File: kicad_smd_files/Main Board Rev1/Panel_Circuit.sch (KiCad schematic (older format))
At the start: 31 parts, among them J12 Conn_01x24_Male, Q1 MMBT3904-7-F, Q2 MMBT3904-7-F, SW2 LEFT/DOWN, SW3 OK, SW4 RIGHT/UP, SW5 MENU, U3 CD4006B

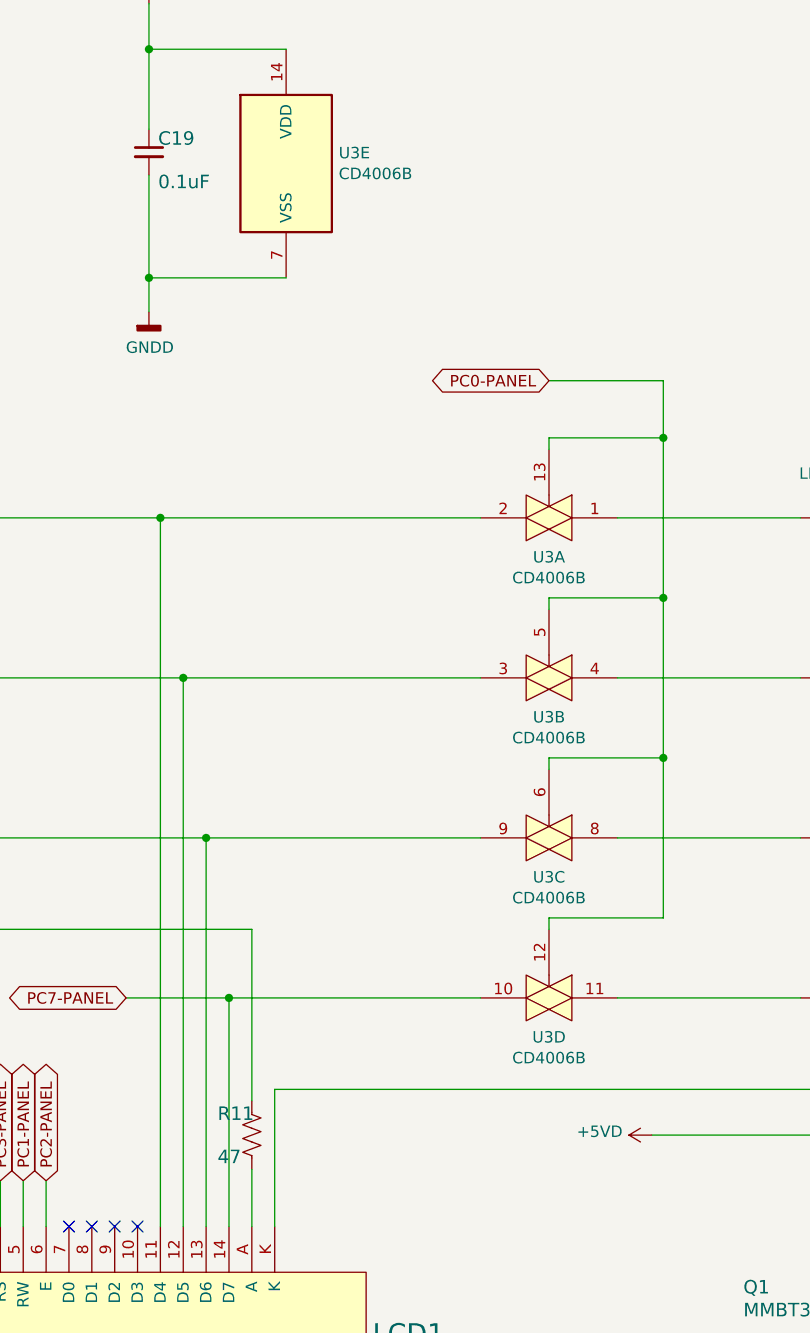
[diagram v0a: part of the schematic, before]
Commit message: Firmware patch to support new LCD, more beefy power circuit for LiPo, added LiPo Balance and protection, fixed reversed op-amp comparitor pins
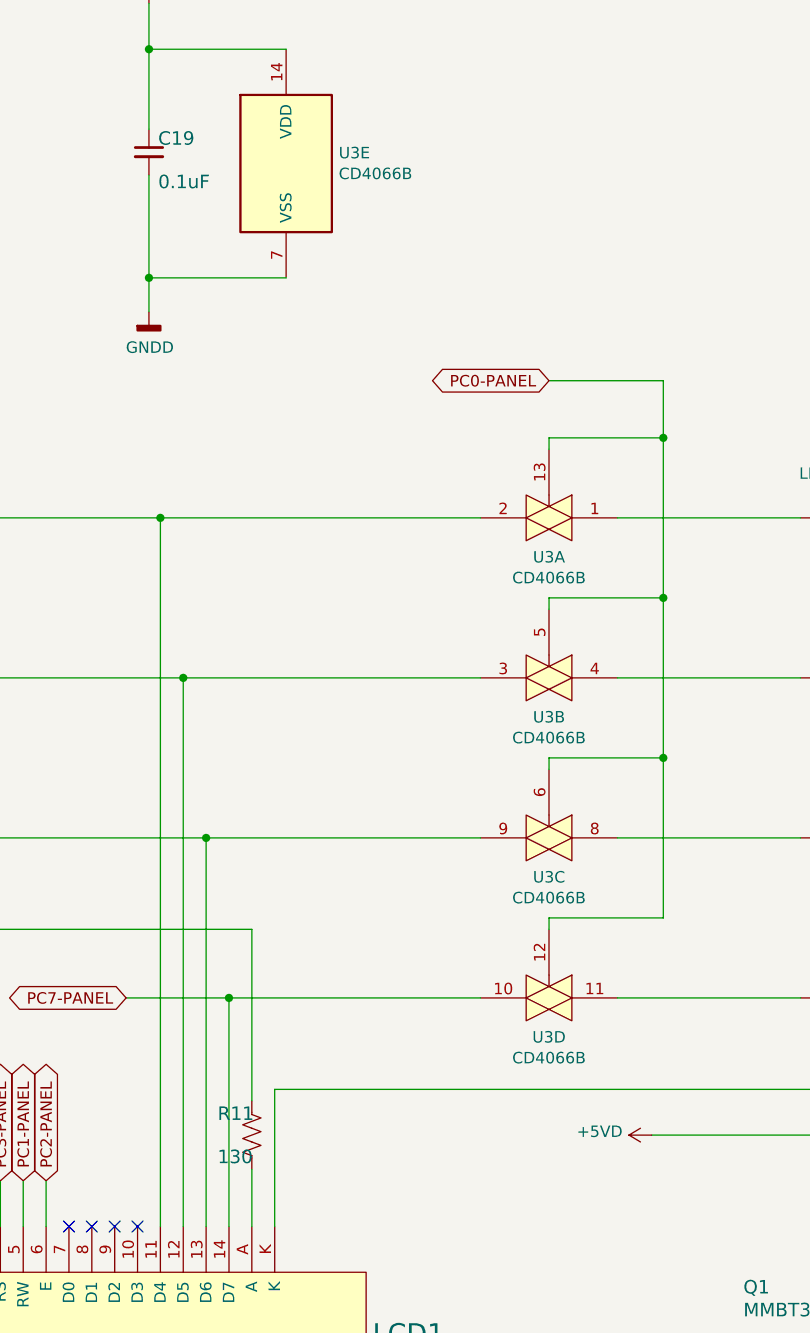
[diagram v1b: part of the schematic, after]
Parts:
- R11: value 47 -> 130; Manufacturer_Name Panasonic -> Yageo; Manufacturer_Part_Number ERJ-PA3F47R0V -> RC0603FR-07130RL; Mouser Part Number 667-ERJ-PA3F47R0V -> 603-RC0603FR-07130RL
- U3: value CD4006B -> CD4066B
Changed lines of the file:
@@
 AR Path="/5CB412A8/BCDF5D1A" Ref="R11"  Part="1"
 F 0 "R11" H 6650 5459 59  0000 L BNN
-F 1 "47" H 6650 5270 59  0000 L BNN
+F 1 "130" H 6650 5270 59  0000 L BNN
 F 2 "Resistor_SMD:R_0603_1608Metric" H 6800 5400 50  0001 C CNN
-F 3 "https://www.mouser.com/datasheet/2/315/AOA0000C331-1141874.pdf" H 6800 5400 50  0001 C CNN
-F 4 "Panasonic" H 6800 5400 50  0001 C CNN "Manufacturer_Name"
-F 5 "ERJ-PA3F47R0V" H 6800 5400 50  0001 C CNN "Manufacturer_Part_Number"
-F 6 "667-ERJ-PA3F47R0V" H 6800 5400 50  0001 C CNN "Mouser Part Number"
+F 3 "" H 6800 5400 50  0001 C CNN
+F 4 "Yageo" H 6800 5400 50  0001 C CNN "Manufacturer_Name"
+F 5 "RC0603FR-07130RL" H 6800 5400 50  0001 C CNN "Manufacturer_Part_Number"
+F 6 "603-RC0603FR-07130RL" H 6800 5400 50  0001 C CNN "Mouser Part Number"
 	1    6800 5400
 	1    0    0    -1
@@
 P 8100 2700
 F 0 "U3" H 8100 2528 50  0000 C CNN
-F 1 "CD4006B" H 8100 2437 50  0000 C CNN
+F 1 "CD4066B" H 8100 2437 50  0000 C CNN
 F 2 "Package_SO:SOIC-14_3.9x8.7mm_P1.27mm" H 8100 2700 50  0001 C CNN
 F 3 "http://www.ti.com/lit/ds/symlink/cd4066b.pdf" H 8100 2700 50  0001 C CNN
@@
 P 8100 3400
 F 0 "U3" H 8100 3228 50  0000 C CNN
-F 1 "CD4006B" H 8100 3137 50  0000 C CNN
+F 1 "CD4066B" H 8100 3137 50  0000 C CNN
 F 2 "Package_SO:SOIC-14_3.9x8.7mm_P1.27mm" H 8100 3400 50  0001 C CNN
 F 3 "http://www.ti.com/lit/ds/symlink/cd4066b.pdf" H 8100 3400 50  0001 C CNN
@@
 P 8100 4100
 F 0 "U3" H 8100 3928 50  0000 C CNN
-F 1 "CD4006B" H 8100 3837 50  0000 C CNN
+F 1 "CD4066B" H 8100 3837 50  0000 C CNN
 F 2 "Package_SO:SOIC-14_3.9x8.7mm_P1.27mm" H 8100 4100 50  0001 C CNN
 F 3 "http://www.ti.com/lit/ds/symlink/cd4066b.pdf" H 8100 4100 50  0001 C CNN
@@
 P 8100 4800
 F 0 "U3" H 8100 4628 50  0000 C CNN
-F 1 "CD4006B" H 8100 4537 50  0000 C CNN
+F 1 "CD4066B" H 8100 4537 50  0000 C CNN
 F 2 "Package_SO:SOIC-14_3.9x8.7mm_P1.27mm" H 8100 4800 50  0001 C CNN
 F 3 "http://www.ti.com/lit/ds/symlink/cd4066b.pdf" H 8100 4800 50  0001 C CNN
@@
 P 6950 1150
 F 0 "U3" H 7180 1196 50  0000 L CNN
-F 1 "CD4006B" H 7180 1105 50  0000 L CNN
+F 1 "CD4066B" H 7180 1105 50  0000 L CNN
 F 2 "Package_SO:SOIC-14_3.9x8.7mm_P1.27mm" H 6950 1150 50  0001 C CNN
 F 3 "http://www.ti.com/lit/ds/symlink/cd4066b.pdf" H 6950 1150 50  0001 C CNN
